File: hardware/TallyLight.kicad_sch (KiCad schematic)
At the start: 6 parts

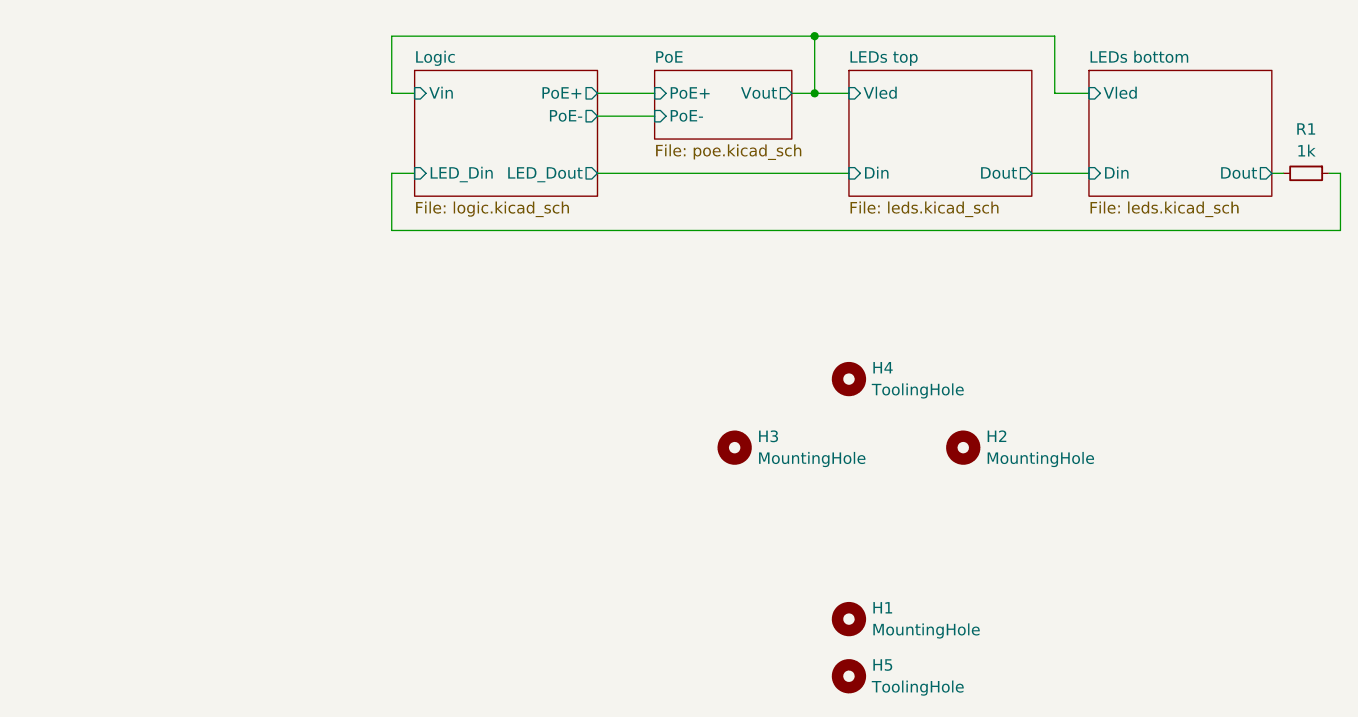
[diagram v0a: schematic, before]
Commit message: hardware: switch to ESP32-C3 MCU and Si3402-B for PoE
Further changes:
 - Enlarge center hole to 16mm diameter
 - Replace Ethernet Phy by KSZ8851 SPI MAC + Phy
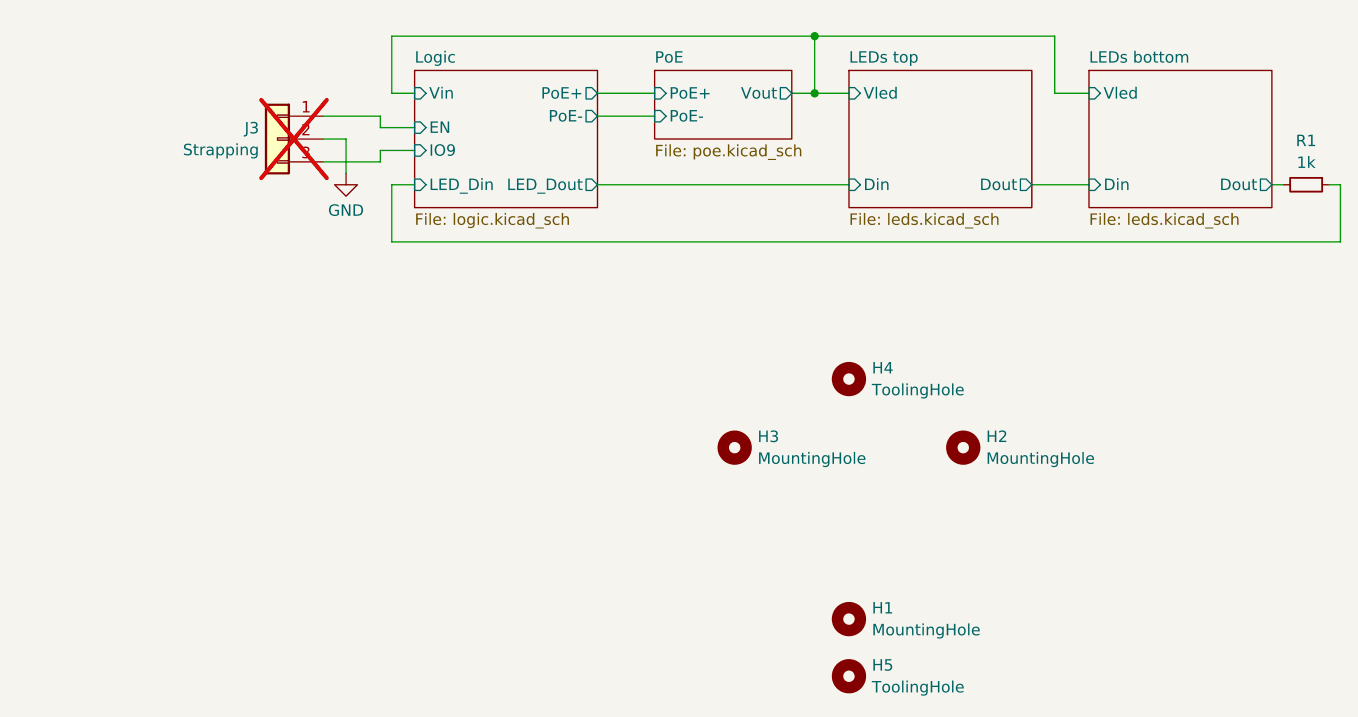
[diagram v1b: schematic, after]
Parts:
- added J3: Strapping, Connector_PinHeader_2.54mm:PinHeader_1x03_P2.54mm_Vertical, symbol Connector_Generic:Conn_01x03
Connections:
- new net GND: J3.2 (Pin_2)
- new net Logic/EN: J3.1 (Pin_1)
- new net Logic/IO9: J3.3 (Pin_3)
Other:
- sheet Logic ports: added EN, IO9; removed none
- moved on the sheet: R1

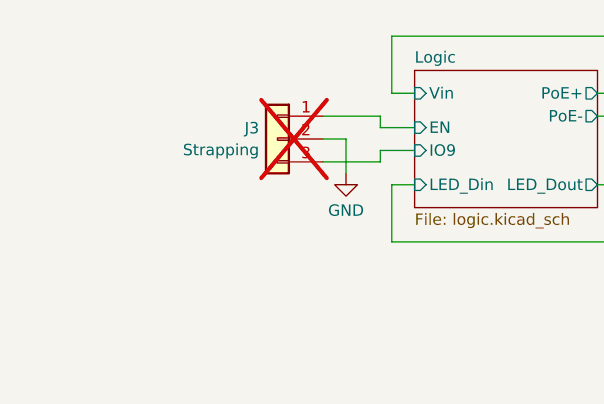
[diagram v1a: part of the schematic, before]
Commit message: hardware: add testpoints to flyback converter and SPI MAC + Phy
Add testpoints to all critical section that might require in-circuit
debugging
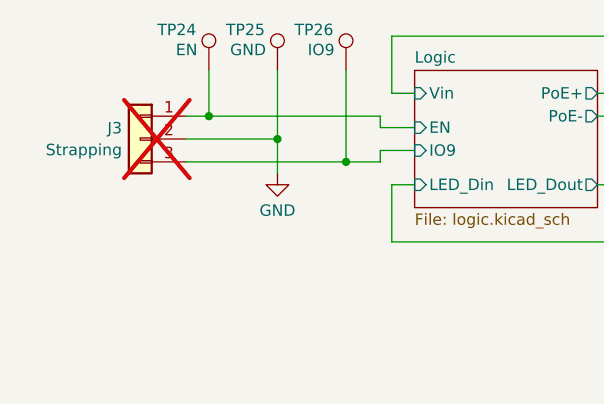
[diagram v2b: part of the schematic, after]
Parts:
- added TP24: EN, TestPoint_no_outline:TestPoint_Pad_D2.0mm_no_outline, symbol Connector:TestPoint
- added TP25: GND, TestPoint:TestPoint_Pad_D2.0mm, symbol Connector:TestPoint
- added TP26: IO9, TestPoint_no_outline:TestPoint_Pad_D2.0mm_no_outline, symbol Connector:TestPoint
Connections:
- net GND: now also TP25.1
- net Logic/EN: now also TP24.1
- net Logic/IO9: now also TP26.1
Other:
- moved on the sheet: J3

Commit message: Exclude parts with virtual footprints from BOM
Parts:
- TP24, TP25, TP26: now left out of the parts list
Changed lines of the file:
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@@
 		(unit 1)
 		(exclude_from_sim no)
-		(in_bom yes)
+		(in_bom no)
 		(on_board yes)
 		(dnp no)
@@
 		(unit 1)
 		(exclude_from_sim no)
-		(in_bom yes)
+		(in_bom no)
 		(on_board yes)
 		(dnp no)
@@
 		(unit 1)
 		(exclude_from_sim no)
-		(in_bom yes)
-		(on_board yes)
-		(dnp no)
+		(in_bom no)
+		(on_board yes)
+		(dnp no)
